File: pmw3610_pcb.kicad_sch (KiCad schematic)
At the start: 24 parts, among them J1 Conn_01x06, J2 Conn_01x08, U1 PMW3610, U2 TLV74318PDBVR

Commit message: feat: update PCB rev 1.1
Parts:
- removed J1: Conn_01x06, Connector_PinHeader_2.54mm:PinHeader_1x06_P2.54mm_Vertical, symbol Connector_Generic:Conn_01x06
- removed TP1: TestPoint, TestPoint:TestPoint_Pad_D1.5mm, symbol Connector:TestPoint
- added J1: Conn_PinHeader, Connector_PinHeader_2.54mm:PinHeader_1x07_P2.54mm_Vertical, symbol Connector_Generic:Conn_01x07
- C1: footprint Capacitor_SMD:C_0603_1608Metric -> Capacitor_SMD:C_0805_2012Metric; JLCPCB Part # (none) -> C7393948; MFR. Part # (none) -> TCC0805X7R335K250FT
- C10: JLCPCB Part # (none) -> C21122; MFR. Part # (none) -> CL10B223KB8NNNC
- C2, C3: JLCPCB Part # (none) -> C14663; MFR. Part # (none) -> CC0603KRX7R9BB104
- C4: value 100nF X7R -> 100nF; JLCPCB Part # (none) -> C14663; MFR. Part # (none) -> CC0603KRX7R9BB104
- C5: JLCPCB Part # (none) -> C57112; MFR. Part # (none) -> 0603B103K500NT
- C6: value 10uF X7R -> 10uF; footprint Capacitor_SMD:C_0603_1608Metric -> Capacitor_SMD:C_0805_2012Metric; JLCPCB Part # (none) -> C15850; MFR. Part # (none) -> CL21A106KAYNNNE
- C7: value 10nF X7R -> 10nF; JLCPCB Part # (none) -> C57112; MFR. Part # (none) -> 0603B103K500NT
- C8, C9: JLCPCB Part # (none) -> C15849; MFR. Part # (none) -> CL10A105KB8NNNC
- H1, H2, H3, H4, JP1, TP2, TP3: now left out of the parts list
- J2: value Conn_01x08 -> Conn_FPC; JLCPCB Part # (none) -> C2856797; MFR. Part # (none) -> FPC-05F-8PH20
- R1: JLCPCB Part # (none) -> C25804; MFR. Part # (none) -> 0603WAF1002T5E; now fitted
- TP1: renamed from TP4; now left out of the parts list
- U1: JLCPCB Part # (none) -> C42442560; MFR. Part # (none) -> PMW3610DM-SUDU
- U2: JLCPCB Part # (none) -> C485152; MFR. Part # (none) -> TLV74318PDBVR
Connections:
- net GND: now also J1.2 (Pin_2)
- net MOTION: now also J1.6 (Pin_6)
- net SCLK: now also J1.4 (Pin_4)
- net SDIO: now also J1.3 (Pin_3)
- net VIN: now also J1.1 (Pin_1)
- net nCS: now also J1.5 (Pin_5)
- net nRESET: now also J2.8 (Pin_8), J1.7 (Pin_7)
- net VIO renamed VDDIO
- no-connect marks 2 -> 1
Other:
- note added: "Connector"
- note added: "Mounting Hole"
- note added: "NC: Not Connected"
- note added: "Power"
- note added: "Sensor"
- note added: "U2 (TLV74318) can be replaced with RT9193-18GB; use 22 nF for C10"
- note added: "VDD: 1.7V~2.1V, 1.8V Typical. VDDIO: 1.7V~3.3V, 1.8V Typical."
- moved on the sheet: C1, C10, C2, C3, C4, C5, C6, C7, C8, C9, H1, H2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

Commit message: feat: update FPC connector symbol
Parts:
- J2: symbol Connector_Generic:Conn_01x08 -> Connector_Generic_MountingPin:Conn_01x08_MountingPin
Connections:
- no-connect marks 1 -> 2
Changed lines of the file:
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@@
 		(at 243.84 66.04)
+	)
+	(no_connect
+		(at 248.92 81.28)
 	)
 	(wire
@@
 	)
 	(symbol
-		(lib_id "Connector_Generic:Conn_01x08")
+		(lib_id "Connector_Generic_MountingPin:Conn_01x08_MountingPin")
 		(at 248.92 66.04 0)
 		(unit 1)
@@
 			)
 		)
-		(property "Description" ""
+		(property "Description" "Generic connectable mounting pin connector, single row, 01x08, script generated (kicad-library-utils/schlib/autogen/connector/)"
 			(at 248.92 66.04 0)
 			(effects
@@
 					(size 1.27 1.27)
 				)
+				(hide yes)
 			)
 		)
@@
 		(pin "8"
 		)
+		(pin "MP"
+		)
 		(instances

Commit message: feat: changed the J2 to the top layer
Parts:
- J2: JLCPCB Part # C2856797 -> C19273926; MFR. Part # FPC-05F-8PH20 -> HC-FPC-0.5-8P-FH20
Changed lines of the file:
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@@
 	(title_block
 		(title "PMW3610 PCB")
-		(rev "1.1")
+		(rev "2.0")
 		(company "SideraKB")
 		(comment 1 "Open Source Hardware, CERN-OHL-P v2")
@@
 			)
 		)
-		(property "JLCPCB Part #" "C2856797"
+		(property "JLCPCB Part #" "C19273926"
 			(at 248.92 66.04 0)
 			(effects
@@
 			)
 		)
-		(property "MFR. Part #" "FPC-05F-8PH20"
+		(property "MFR. Part #" "HC-FPC-0.5-8P-FH20"
 			(at 248.92 66.04 0)
 			(effects

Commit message: feat: update part number of J2
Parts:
- J2: JLCPCB Part # C19273926 -> C262657; MFR. Part # HC-FPC-0.5-8P-FH20 -> AFC01-S08FCA-00
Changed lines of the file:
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@@
 			)
 		)
-		(property "JLCPCB Part #" "C19273926"
+		(property "JLCPCB Part #" "C262657"
 			(at 248.92 66.04 0)
 			(effects
@@
 			)
 		)
-		(property "MFR. Part #" "HC-FPC-0.5-8P-FH20"
+		(property "MFR. Part #" "AFC01-S08FCA-00"
 			(at 248.92 66.04 0)
 			(effects

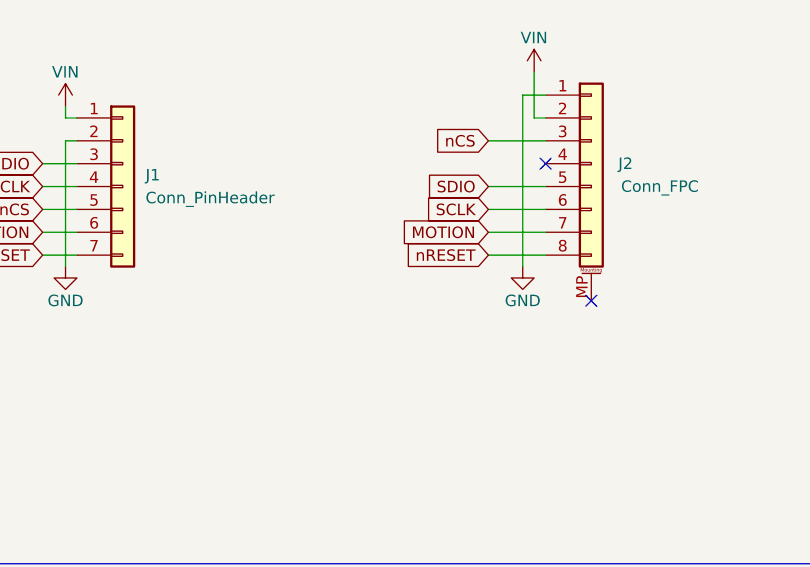
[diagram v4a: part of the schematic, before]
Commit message: feat: add jumper JP2 for FFC/FPC and nRESET pin
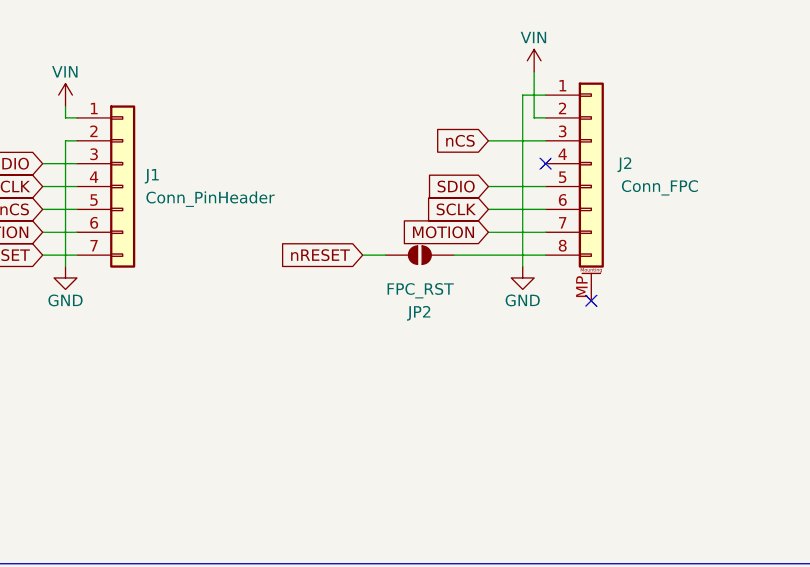
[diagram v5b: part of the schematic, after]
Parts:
- added JP2: FPC_RST, Jumper:SolderJumper-2_P1.3mm_Open_RoundedPad1.0x1.5mm, symbol Jumper:SolderJumper_2_Open
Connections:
- net nRESET: now also JP2.1 (A); no longer J2.8 (Pin_8)
- new net: J2.8 (Pin_8), JP2.2 (B)
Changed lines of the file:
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@@
 	(title_block
 		(title "PMW3610 PCB")
-		(rev "2.0")
+		(rev "2.1")
 		(company "SideraKB")
 		(comment 1 "Open Source Hardware, CERN-OHL-P v2")
@@
 	(wire
 		(pts
+			(xy 223.52 76.2) (xy 226.06 76.2)
+		)
+		(stroke
+			(width 0)
+			(type default)
+		)
+	)
+	(wire
+		(pts
 			(xy 54.61 157.48) (xy 66.04 157.48)
 		)
@@
 	(wire
 		(pts
-			(xy 237.49 76.2) (xy 243.84 76.2)
+			(xy 233.68 76.2) (xy 243.84 76.2)
 		)
 		(stroke
@@
 		)
 	)
+	(global_label "nRESET"
+		(shape input)
+		(at 223.52 76.2 180)
+		(fields_autoplaced yes)
+		(effects
+			(font
+				(size 1.27 1.27)
+			)
+			(justify right)
+		)
+		(property "Intersheetrefs" "${INTERSHEET_REFS}"
+			(at 213.6407 76.2 0)
+			(effects
+				(font
+					(size 1.27 1.27)
+				)
+				(justify right)
+				(hide yes)
+			)
+		)
+	)
 	(global_label "MOTION"
 		(shape input)
@@
 		(property "Intersheetrefs" "${INTERSHEET_REFS}"
 			(at 229.7272 71.12 0)
-			(effects
-				(font
-					(size 1.27 1.27)
-				)
-				(justify right)
-				(hide yes)
-			)
-		)
-	)
-	(global_label "nRESET"
-		(shape input)
-		(at 237.49 76.2 180)
-		(fields_autoplaced yes)
-		(effects
-			(font
-				(size 1.27 1.27)
-			)
-			(justify right)
-		)
-		(property "Intersheetrefs" "${INTERSHEET_REFS}"
-			(at 227.6107 76.2 0)
 			(effects
 				(font
@@
 					(unit 1)
 				)
+			)
+		)
+	)
+	(symbol
+		(lib_id "Jumper:SolderJumper_2_Open")
+		(at 229.87 76.2 0)
+		(mirror x)
+		(unit 1)
+		(exclude_from_sim no)
+		(in_bom no)
+		(on_board yes)
+		(dnp no)
+		(property "Reference" "JP2"
+			(at 229.87 82.55 0)
+			(effects
+				(font
+					(size 1.27 1.27)
+				)
+			)
+		)
+		(property "Value" "FPC_RST"
+			(at 229.87 80.01 0)
+			(effects
+				(font
+					(size 1.27 1.27)
+				)
+			)
+		)
+		(property "Footprint" "Jumper:SolderJumper-2_P1.3mm_Open_RoundedPad1.0x1.5mm"
+			(at 229.87 76.2 0)
+			(effects
+				(font
+					(size 1.27 1.27)
+				)
+				(hide yes)
+			)
+		)
+		(property "Datasheet" "~"
+			(at 229.87 76.2 0)
+			(effects
+				(font
+					(size 1.27 1.27)
+				)
+				(hide yes)
+			)
+		)
+		(property "Description" "Solder Jumper, 2-pole, open"
+			(at 229.87 76.2 0)
+			(effects
+				(font
+					(size 1.27 1.27)
+				)
+				(hide yes)
+			)
+		)
+		(pin "2"
+		)
+		(pin "1"
+		)
+		(instances
+			(project ""
+				(path "/0a24e726-7b2f-42a2-8e64-ccc5f26dfd32"
+					(reference "JP2")
+					(unit 1)
+				)

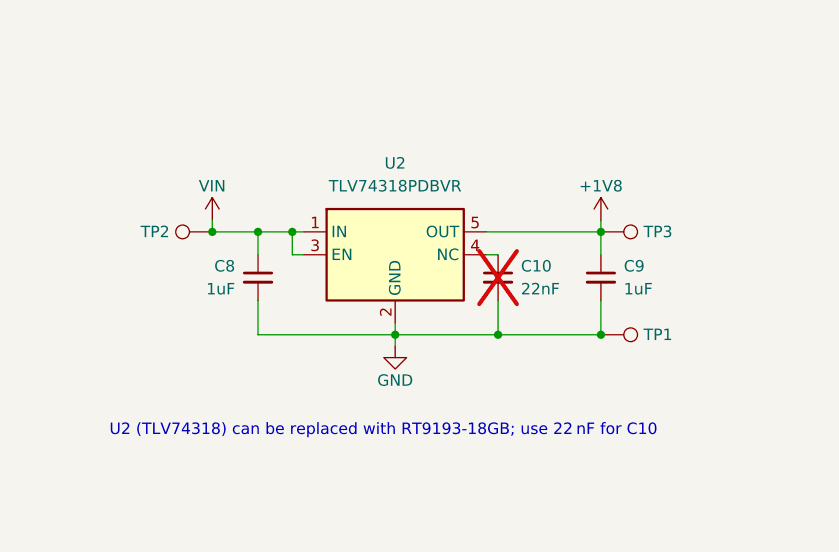
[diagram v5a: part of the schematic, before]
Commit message: feat: add top silkscreen header labels and reroute traces
What this commit
  contains:

  - Adds readable top-side header labels for J1 for soldering.
  - Updates board/schematic revision to 2.2.
  - Reroutes traces and nearby items to fit the silkscreen labels.
  - Swaps TP1/TP2 placement intentionally for routing, with schematic and PCB matching.
  - Includes the KiCad 10 project update in .kicad_pro.
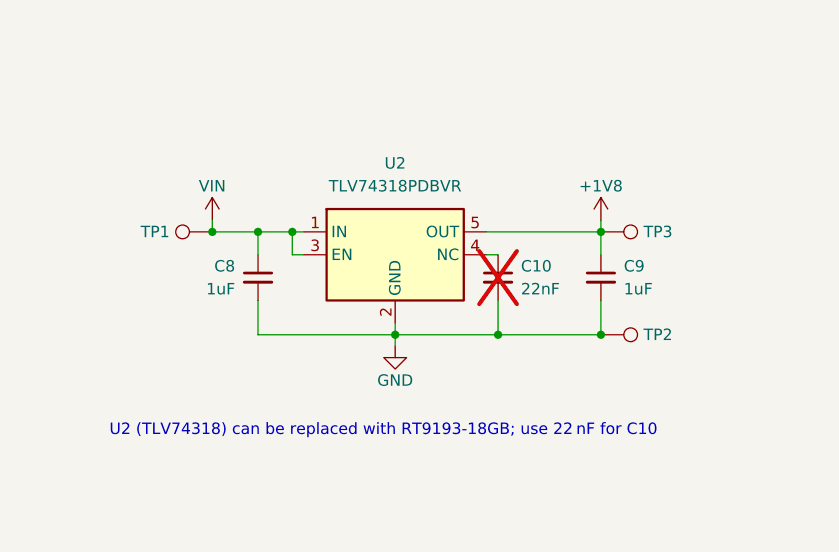
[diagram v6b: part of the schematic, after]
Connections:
- net GND: now also TP2.1; no longer TP1.1
- net VIN: now also TP1.1; no longer TP2.1
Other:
- moved on the sheet: TP1, TP2

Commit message: fix: correct assembly metadata and FPC footprint origin
What this commit
  contains:

  - Excludes J1 from PCB assembly BOM/position outputs so JLC does not place the header.
  - Excludes C10 from BOM/position outputs while leaving it DNP.
  - Corrects the J2 FPC footprint origin so JLC placement previews correctly.
  - Updates the local FPC footprint library and placed footprint to match.
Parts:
- C10: now left out of the parts list
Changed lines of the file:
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@@
 		(body_style 1)
 		(exclude_from_sim no)
-		(in_bom yes)
+		(in_bom no)
 		(on_board yes)
-		(in_pos_files yes)
+		(in_pos_files no)
 		(dnp yes)
 		(property "Reference" "C10"
